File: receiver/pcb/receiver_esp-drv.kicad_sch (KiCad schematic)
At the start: 20 parts, among them J1 Conn_01x02_Female, J2 Conn_01x02_Female, J3 Conn_01x02_Female, J4 Conn_01x01_Female-weapon, J5 Conn_01x01_Female-weapon, U1 DRV8870DDA, U2 DRV8870DDA, U3 AMS1117-3.3, U4 ESP32-C3-MINI-1

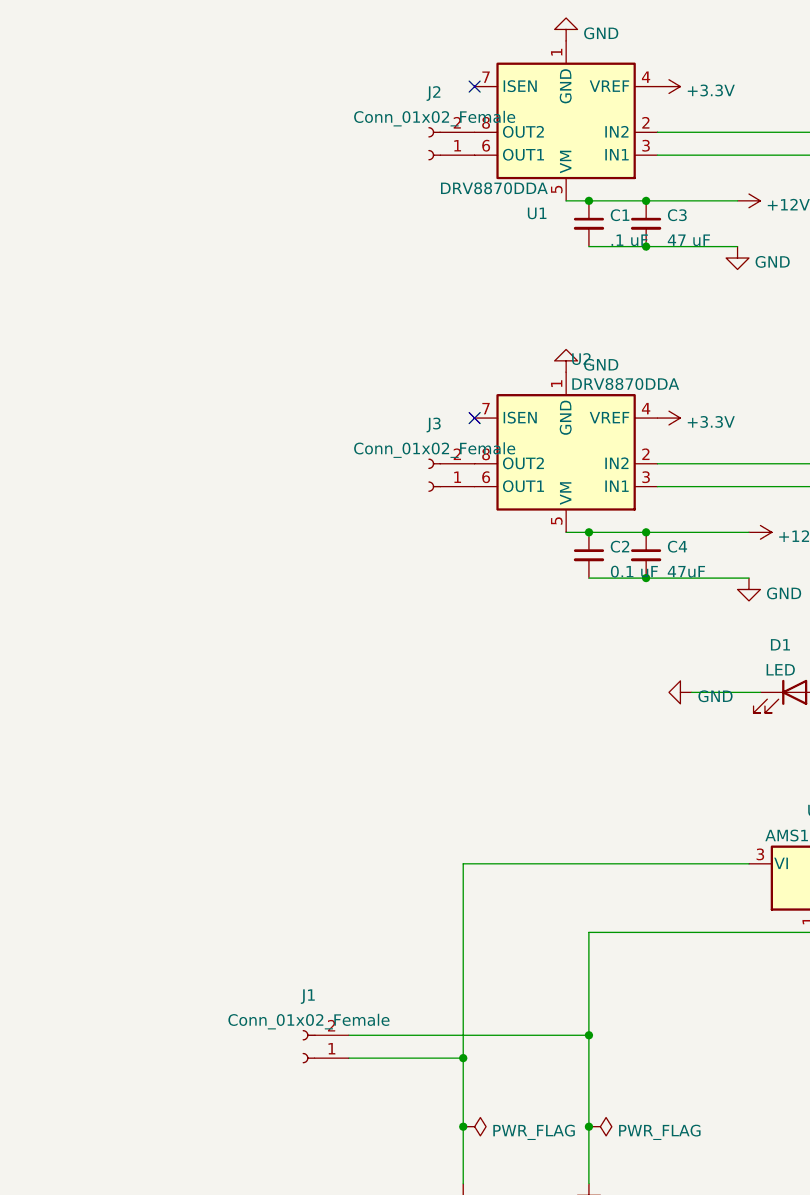
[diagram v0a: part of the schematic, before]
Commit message: increase trace width on receiver pcb
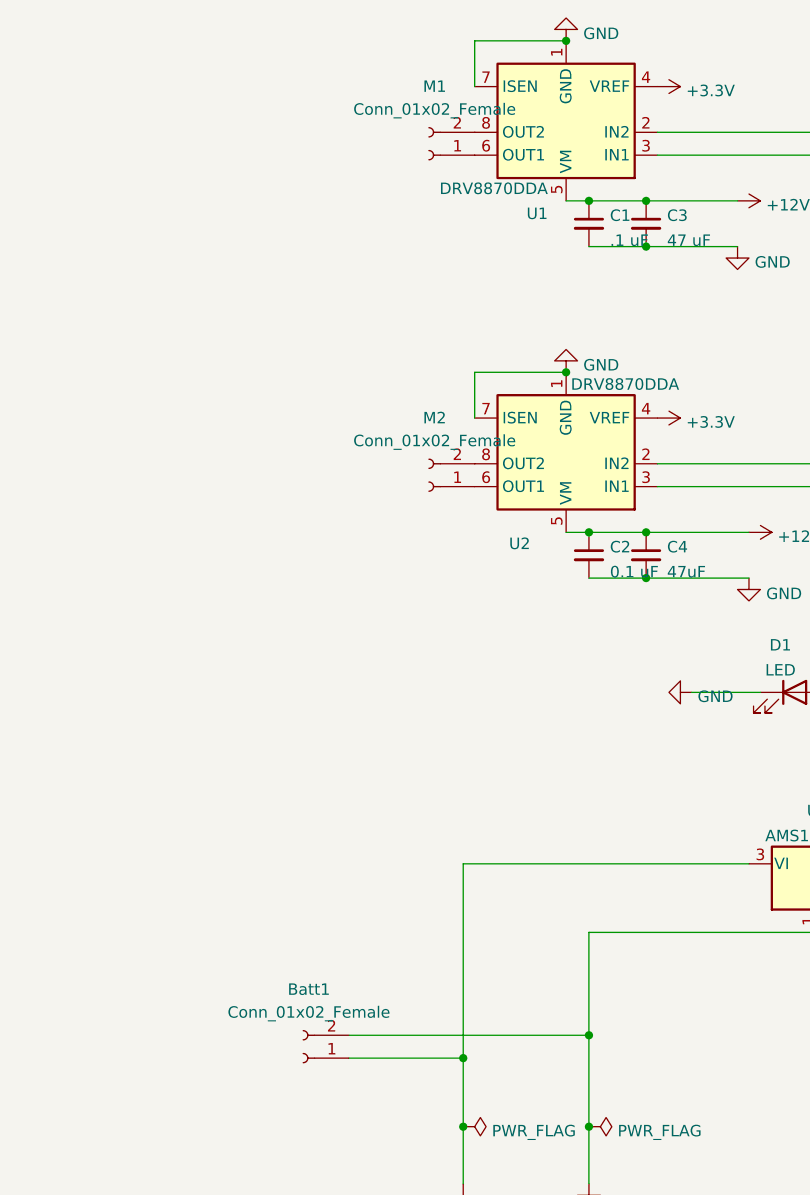
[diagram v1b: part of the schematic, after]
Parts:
- renumbered J1 to Batt1, J2 to M1, J3 to M2
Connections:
- net GND: now also U1.7 (ISEN), U2.7 (ISEN)
- no-connect marks 12 -> 10
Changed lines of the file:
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@@
   (junction (at 151.13 105.41) (diameter 0) (color 0 0 0 0)
+  )
+  (junction (at 142.24 50.8) (diameter 0) (color 0 0 0 0)
+  )
+  (junction (at 142.24 87.63) (diameter 0) (color 0 0 0 0)
   )
   (junction (at 151.13 110.49) (diameter 0) (color 0 0 0 0)
@@
   (no_connect (at 205.74 96.52))
   (no_connect (at 205.74 99.06))
-  (no_connect (at 132.08 55.88))
-  (no_connect (at 132.08 92.71))
   (wire (pts (xy 144.78 110.49) (xy 151.13 110.49))
     (stroke (width 0) (type default) (color 0 0 0 0))
@@
     (stroke (width 0) (type default) (color 0 0 0 0))
   )
+  (wire (pts (xy 132.08 50.8) (xy 132.08 55.88))
+    (stroke (width 0) (type default) (color 0 0 0 0))
+  )
   (wire (pts (xy 193.04 60.96) (xy 152.4 60.96))
     (stroke (width 0) (type default) (color 0 0 0 0))
@@
     (stroke (width 0) (type default) (color 0 0 0 0))
   )
+  (wire (pts (xy 142.24 50.8) (xy 132.08 50.8))
+    (stroke (width 0) (type default) (color 0 0 0 0))
+  )
   (wire (pts (xy 205.74 83.82) (xy 193.04 83.82))
     (stroke (width 0) (type default) (color 0 0 0 0))
@@
     (stroke (width 0) (type default) (color 0 0 0 0))
   )
+  (wire (pts (xy 132.08 87.63) (xy 132.08 92.71))
+    (stroke (width 0) (type default) (color 0 0 0 0))
+  )
   (wire (pts (xy 198.12 88.9) (xy 198.12 123.19))
     (stroke (width 0) (type default) (color 0 0 0 0))
@@
   )
   (wire (pts (xy 130.81 142.24) (xy 130.81 163.83))
+    (stroke (width 0) (type default) (color 0 0 0 0))
+  )
+  (wire (pts (xy 142.24 87.63) (xy 132.08 87.63))
     (stroke (width 0) (type default) (color 0 0 0 0))
   )
@@
   (symbol (lib_id "Connector:Conn_01x02_Female") (at 127 63.5 180) (unit 1)
     (in_bom yes) (on_board yes) (fields_autoplaced)
-    (property "Reference" "J2" (id 0) (at 127.635 56.5363 0))
-    (property "Value" "Conn_01x02_Female" (id 1) (at 127.635 59.3114 0))
+    (property "Reference" "M1" (id 0) (at 127.635 55.88 0))
+    (property "Value" "Conn_01x02_Female" (id 1) (at 127.635 58.42 0))
     (property "Footprint" "Connector_PinSocket_2.54mm:PinSocket_1x02_P2.54mm_Vertical" (id 2) (at 127 63.5 0)
       (effects (font (size 1.27 1.27)) hide)
@@
   )
   (symbol (lib_id "Driver_Motor:DRV8870DDA") (at 142.24 97.79 180) (unit 1)
-    (in_bom yes) (on_board yes) (fields_autoplaced)
-    (property "Reference" "U2" (id 0) (at 142.7606 86.2035 0)
+    (in_bom yes) (on_board yes)
+    (property "Reference" "U2" (id 0) (at 135.89 106.68 0)
       (effects (font (size 1.27 1.27)) (justify right))
     )
@@
   (symbol (lib_id "Connector:Conn_01x02_Female") (at 113.03 163.83 180) (unit 1)
     (in_bom yes) (on_board yes) (fields_autoplaced)
-    (property "Reference" "J1" (id 0) (at 113.665 156.8663 0))
-    (property "Value" "Conn_01x02_Female" (id 1) (at 113.665 159.6414 0))
+    (property "Reference" "Batt1" (id 0) (at 113.665 156.21 0))
+    (property "Value" "Conn_01x02_Female" (id 1) (at 113.665 158.75 0))
     (property "Footprint" "Connector_PinSocket_2.54mm:PinSocket_1x02_P2.54mm_Vertical" (id 2) (at 113.03 163.83 0)
       (effects (font (size 1.27 1.27)) hide)
@@
   (symbol (lib_id "Connector:Conn_01x02_Female") (at 127 100.33 180) (unit 1)
     (in_bom yes) (on_board yes) (fields_autoplaced)
-    (property "Reference" "J3" (id 0) (at 127.635 93.3663 0))
-    (property "Value" "Conn_01x02_Female" (id 1) (at 127.635 96.1414 0))
+    (property "Reference" "M2" (id 0) (at 127.635 92.71 0))
+    (property "Value" "Conn_01x02_Female" (id 1) (at 127.635 95.25 0))
     (property "Footprint" "Connector_PinSocket_2.54mm:PinSocket_1x02_P2.54mm_Vertical" (id 2) (at 127 100.33 0)
       (effects (font (size 1.27 1.27)) hide)
@@
       (reference "#PWR014") (unit 1) (value "GND") (footprint "")
     )
+    (path "/af7d5969-1c54-438c-a84c-b4fb60a98280"
+      (reference "Batt1") (unit 1) (value "Conn_01x02_Female") (footprint "Connector_PinSocket_2.54mm:PinSocket_1x02_P2.54mm_Vertical")
+    )
     (path "/d92df7aa-b105-477e-a3a0-b3a952577ad5"
       (reference "C1") (unit 1) (value ".1 uF") (footprint "Capacitor_SMD:C_0805_2012Metric_Pad1.18x1.45mm_HandSolder")
@@
       (reference "H4") (unit 1) (value "MountingHole") (footprint "MountingHole:MountingHole_3.2mm_M3")
     )
-    (path "/af7d5969-1c54-438c-a84c-b4fb60a98280"
-      (reference "J1") (unit 1) (value "Conn_01x02_Female") (footprint "Connector_PinSocket_2.54mm:PinSocket_1x02_P2.54mm_Vertical")
-    )
-    (path "/70334f67-9f0b-4d5d-8060-8394979c3fb5"
-      (reference "J2") (unit 1) (value "Conn_01x02_Female") (footprint "Connector_PinSocket_2.54mm:PinSocket_1x02_P2.54mm_Vertical")
-    )
-    (path "/bcd4ce4b-9abc-48f4-a2a4-d58c4f07e782"
-      (reference "J3") (unit 1) (value "Conn_01x02_Female") (footprint "Connector_PinSocket_2.54mm:PinSocket_1x02_P2.54mm_Vertical")
-    )
     (path "/b872abb2-418e-4450-9933-aa26f18d4a14"
       (reference "J4") (unit 1) (value "Conn_01x01_Female-weapon") (footprint "Connector_PinSocket_2.54mm:PinSocket_1x01_P2.54mm_Vertical")
@@
       (reference "J5") (unit 1) (value "Conn_01x01_Female-weapon") (footprint "Connector_PinSocket_2.54mm:PinSocket_1x01_P2.54mm_Vertical")
     )
+    (path "/70334f67-9f0b-4d5d-8060-8394979c3fb5"
+      (reference "M1") (unit 1) (value "Conn_01x02_Female") (footprint "Connector_PinSocket_2.54mm:PinSocket_1x02_P2.54mm_Vertical")
+    )
+    (path "/bcd4ce4b-9abc-48f4-a2a4-d58c4f07e782"
+      (reference "M2") (unit 1) (value "Conn_01x02_Female") (footprint "Connector_PinSocket_2.54mm:PinSocket_1x02_P2.54mm_Vertical")
+    )
     (path "/27a854ec-199a-4b47-b571-3a281b2a645f"

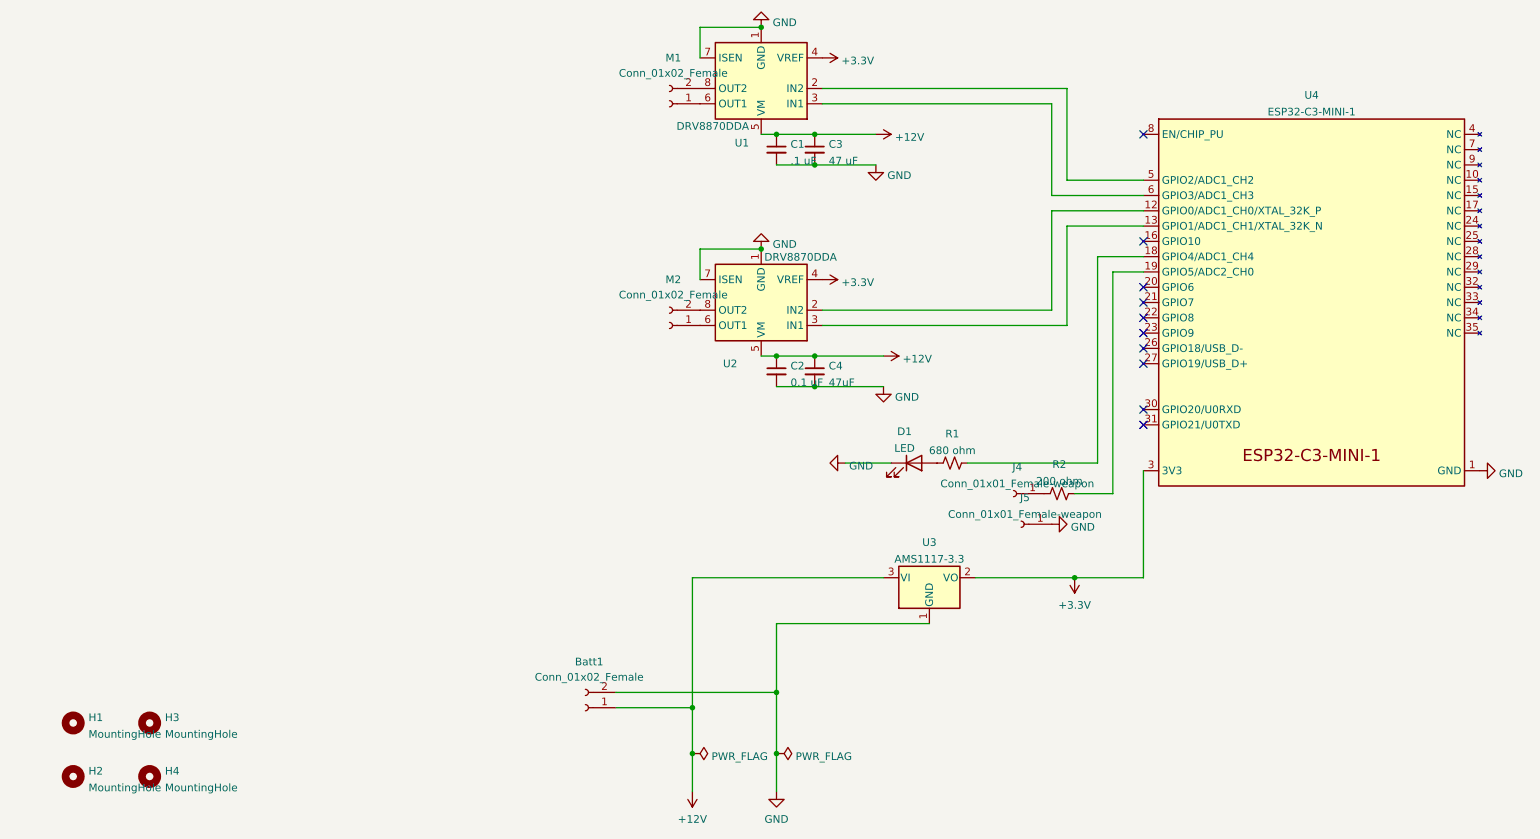
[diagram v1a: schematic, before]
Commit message: add logo footprint
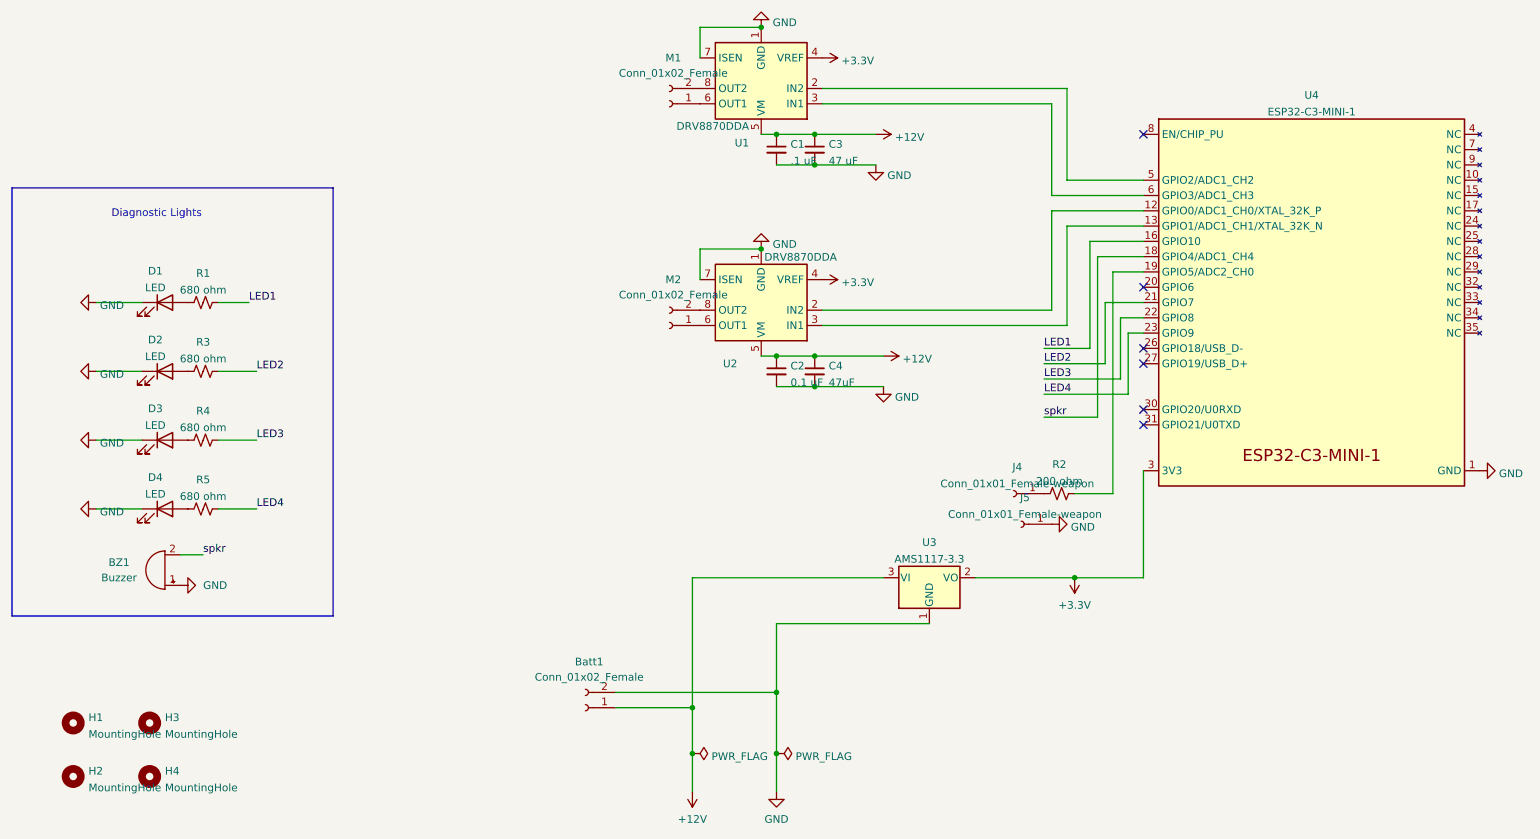
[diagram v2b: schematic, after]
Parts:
- added BZ1: Buzzer, Buzzer_Beeper:Buzzer_CUI_CPT-9019S-SMT, symbol Device:Buzzer
- added D2, D3, D4: LED, LED_SMD:LED_0805_2012Metric_Pad1.15x1.40mm_HandSolder, symbol Device:LED
- added R3, R4, R5: 680 ohm, Resistor_SMD:R_0805_2012Metric_Pad1.20x1.40mm_HandSolder, symbol Device:R_Small_US
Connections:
- net GND: now also BZ1.1 (-), D2.1 (K), D3.1 (K), D4.1 (K)
- net LED1: now reaches R1.1
- net LED1: now also U4.16 (GPIO10); no longer U4.18 (GPIO4/ADC1_CH4)
- net LED2: now reaches U4.21 (GPIO7)
- net LED2: now also R3.1
- net LED3: now reaches U4.22 (GPIO8)
- net LED3: now also R4.1
- net LED4: now reaches U4.23 (GPIO9)
- net LED4: now also R5.1
- new net: D4.2 (A), R5.2
- new net: D3.2 (A), R4.2
- new net: D2.2 (A), R3.2
- new net spkr: BZ1.2 (+), U4.18 (GPIO4/ADC1_CH4)
- no-connect marks 10 -> 6
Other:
- note added: "Diagnostic Lights"
